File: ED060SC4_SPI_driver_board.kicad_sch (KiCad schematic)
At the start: 38 parts, among them J2 Conn_01x06, J3 Conn_01x04, J4 Conn_01x04, J5 Conn_01x06, SW1 SS12D07VG2, SW2 DSIC01LSGET, U2 STM32F103C8T6, U3 USBLC6-4SC6, U4 USBLC6-2SC6, U5 USBLC6-2SC6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

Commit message: TPS Connector and LCSC part #
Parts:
- added J6: Conn_01x02, Connector_PinSocket_2.54mm:PinSocket_1x02_P2.54mm_Vertical, symbol Connector_Generic:Conn_01x02
- C20, C21, C22, C23, C28: LCSC Part # (none) -> C1591
- C24: LCSC Part # (none) -> C85713
- C25: LCSC Part # (none) -> C1589
- C26, C27: LCSC Part # (none) -> C5673
- C29, C30: LCSC Part # (none) -> C1634
- D2: LCSC Part # (none) -> C82544
- FB1: LCSC Part # (none) -> C14709
- R10, R12, R14: LCSC Part # (none) -> C98220
- R3: LCSC Part # (none) -> C22548
- R5: LCSC Part # (none) -> C103196
- SW1: LCSC Part # (none) -> C2939724
- SW2: LCSC Part # (none) -> C54948
- U2: LCSC Part # (none) -> C8734
- U3: LCSC Part # (none) -> C5197386
- U4, U5: LCSC Part # (none) -> C2827654
- Y1: LCSC Part # (none) -> C112972
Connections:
- net SWCLK: no longer J4.2 (Pin_2), U4.3 (I/O2)
- net SWDIO: no longer J4.3 (Pin_3), U4.1 (I/O1)
- net TPS_PWRUP: now also J6.1 (Pin_1)
- net TPS_WAKEUP: now also J6.2 (Pin_2)
- net USART1_RX: no longer J3.3 (Pin_3), U5.1 (I/O1)
- net USART1_TX: no longer J3.2 (Pin_2), U5.3 (I/O2)
- new net SWCLK_conn: J4.2 (Pin_2), U4.3 (I/O2)
- new net SWDIO_conn: J4.3 (Pin_3), U4.1 (I/O1)
- new net USART1_RX_conn: J3.3 (Pin_3), U5.1 (I/O1)
- new net USART1_TX_conn: J3.2 (Pin_2), U5.3 (I/O2)
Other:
- moved on the sheet: TP8, TP9

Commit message: Updated TPS pad for heat dissipation
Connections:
- net PWR_ON_LED_1: now reaches R3.1, SW2.2
- net PWR_ON_LED renamed PWR_ON_LED_0
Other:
- moved on the sheet: R3
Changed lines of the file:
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@@
+    (stroke (width 0) (type default))
+  )
+  (wire (pts (xy 81.28 55.88) (xy 81.28 52.07))
     (stroke (width 0) (type default))
   )
@@
     (stroke (width 0) (type default))
   )
+  (wire (pts (xy 190.5 88.9) (xy 208.28 88.9))
+    (stroke (width 0) (type default))
+  )
+  (wire (pts (xy 16.51 109.22) (xy 31.75 109.22))
+    (stroke (width 0) (type default))
+  )
+  (wire (pts (xy 24.13 55.88) (xy 36.83 55.88))
+    (stroke (width 0) (type default))
+  )
+  (wire (pts (xy 190.5 86.36) (xy 208.28 86.36))
+    (stroke (width 0) (type default))
+  )
   (wire (pts (xy 72.39 36.83) (xy 81.28 36.83))
-    (stroke (width 0) (type default))
-  )
-  (wire (pts (xy 190.5 88.9) (xy 208.28 88.9))
-    (stroke (width 0) (type default))
-  )
-  (wire (pts (xy 16.51 109.22) (xy 31.75 109.22))
-    (stroke (width 0) (type default))
-  )
-  (wire (pts (xy 24.13 55.88) (xy 36.83 55.88))
-    (stroke (width 0) (type default))
-  )
-  (wire (pts (xy 190.5 86.36) (xy 208.28 86.36))
     (stroke (width 0) (type default))
   )
@@
     (effects (font (size 1.27 1.27)) (justify right bottom))
   )
-  (label "PWR_ON_LED" (at 74.93 36.83 0) (fields_autoplaced)
+  (label "PWR_ON_LED_0" (at 73.66 36.83 0) (fields_autoplaced)
     (effects (font (size 0.7 0.7)) (justify left bottom))
   )
@@
   (label "SPI1_MISO" (at 36.83 53.34 180) (fields_autoplaced)
     (effects (font (size 1.27 1.27)) (justify right bottom))
+  )
+  (label "PWR_ON_LED_1" (at 81.28 53.34 180) (fields_autoplaced)
+    (effects (font (size 0.7 0.7)) (justify right bottom))
   )
   (label "D3" (at 270.51 129.54 180) (fields_autoplaced)
@@
     )
   )
-  (symbol (lib_id "power:GND") (at 81.28 59.69 0) (unit 1)
+  (symbol (lib_id "power:GND") (at 81.28 63.5 0) (unit 1)
     (in_bom yes) (on_board yes) (dnp no) (fields_autoplaced)
-    (property "Reference" "#PWR077" (at 81.28 66.04 0)
-      (effects (font (size 1.27 1.27)) hide)
-    )
-    (property "Value" "GND" (at 81.28 64.77 0)
-      (effects (font (size 1.27 1.27)) hide)
-    )
-    (property "Footprint" "" (at 81.28 59.69 0)
-      (effects (font (size 1.27 1.27)) hide)
-    )
-    (property "Datasheet" "" (at 81.28 59.69 0)
+    (property "Reference" "#PWR077" (at 81.28 69.85 0)
+      (effects (font (size 1.27 1.27)) hide)
+    )
+    (property "Value" "GND" (at 81.28 68.58 0)
+      (effects (font (size 1.27 1.27)) hide)
+    )
+    (property "Footprint" "" (at 81.28 63.5 0)
+      (effects (font (size 1.27 1.27)) hide)
+    )
+    (property "Datasheet" "" (at 81.28 63.5 0)
       (effects (font (size 1.27 1.27)) hide)
     )
@@
     )
   )
-  (symbol (lib_id "Device:R") (at 81.28 55.88 0) (unit 1)
-    (in_bom yes) (on_board yes) (dnp no)
-    (property "Reference" "R3" (at 82.55 54.61 0)
-      (effects (font (size 1.27 1.27)) (justify left))
-    )
-    (property "Value" "1k" (at 82.55 57.15 0)
-      (effects (font (size 1.27 1.27)) (justify left))
-    )
-    (property "Footprint" "Resistor_SMD:R_0603_1608Metric" (at 79.502 55.88 90)
-      (effects (font (size 1.27 1.27)) hide)
-    )
-    (property "Datasheet" "~" (at 81.28 55.88 0)
-      (effects (font (size 1.27 1.27)) hide)
-    )
-    (property "LCSC Part #" "C22548" (at 81.28 55.88 0)
-      (effects (font (size 1.27 1.27)) hide)
-    )
+  (symbol (lib_id "Device:R") (at 81.28 59.69 0) (unit 1)
+    (in_bom yes) (on_board yes) (dnp no)
+    (property "Reference" "R3" (at 82.55 58.42 0)
+      (effects (font (size 1.27 1.27)) (justify left))
+    )
+    (property "Value" "1k" (at 82.55 60.96 0)
+      (effects (font (size 1.27 1.27)) (justify left))
+    )
+    (property "Footprint" "Resistor_SMD:R_0603_1608Metric" (at 79.502 59.69 90)
+      (effects (font (size 1.27 1.27)) hide)
+    )
+    (property "Datasheet" "~" (at 81.28 59.69 0)
+      (effects (font (size 1.27 1.27)) hide)
+    )
+    (property "LCSC Part #" "C22548" (at 81.28 59.69 0)
+      (effects (font (size 1.27 1.27)) hide)
+    )

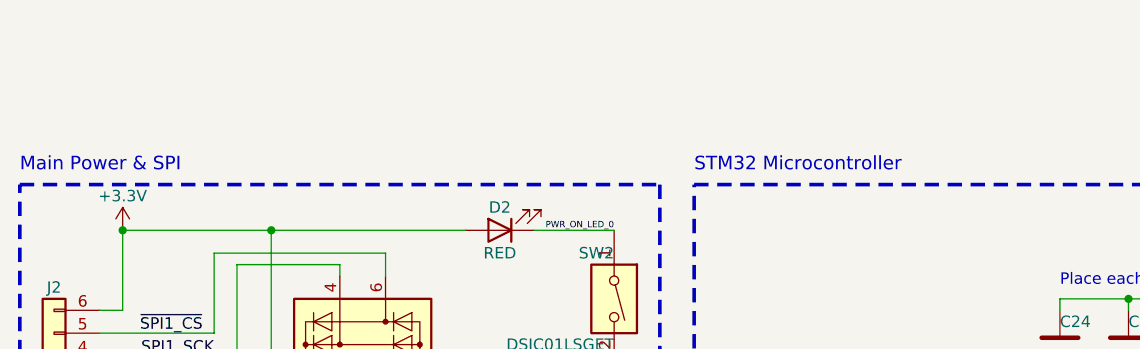
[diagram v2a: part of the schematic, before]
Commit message: Add titles to schematics
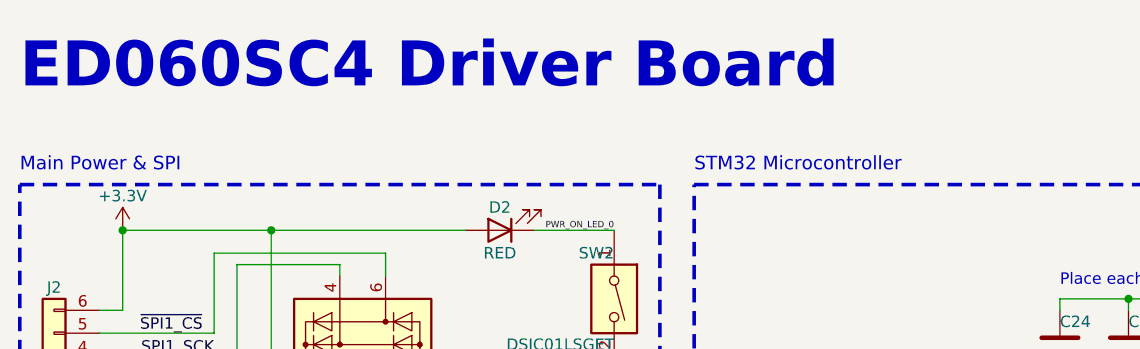
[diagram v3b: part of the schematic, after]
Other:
- note added: "ED060SC4 Driver Board"
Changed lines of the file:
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@@
     (effects (font (size 1.27 1.27)) (justify left bottom))
+  )
+  (text "ED060SC4 Driver Board\n" (at 15.24 21.59 0)
+    (effects (font (size 5 5) (thickness 1.2) bold) (justify left bottom))
   )
   (text "Serial Wire Debug\n\n" (at 15.24 165.1 0)

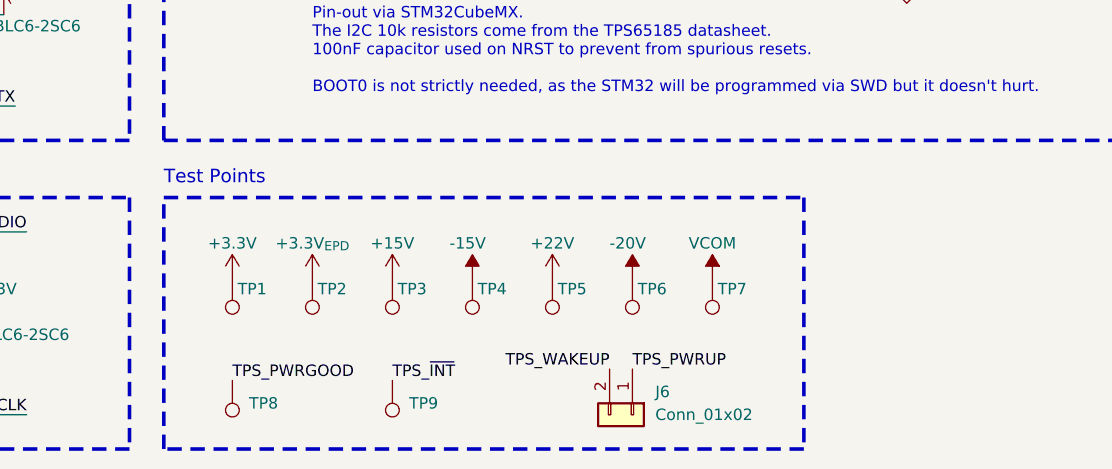
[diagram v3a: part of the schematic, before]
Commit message: Add mounting holes
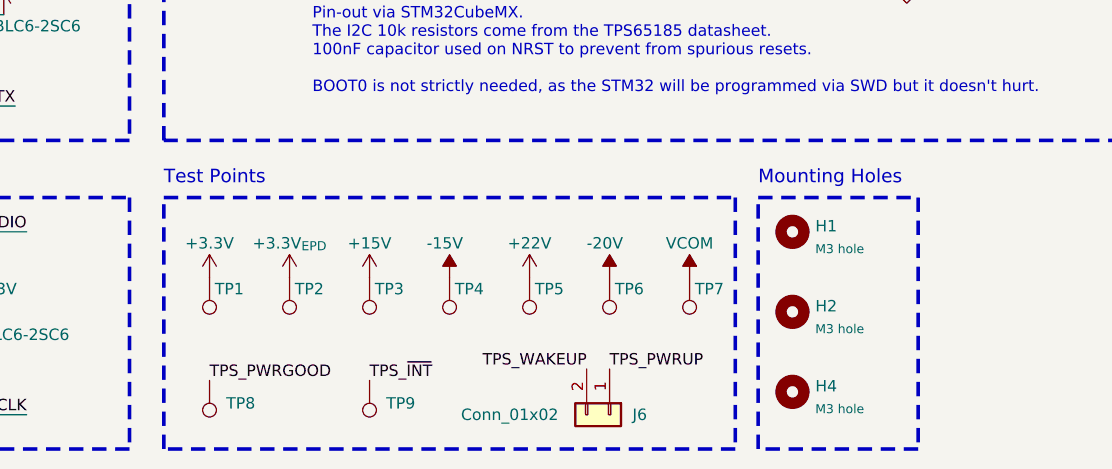
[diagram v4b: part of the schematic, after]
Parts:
- added H1, H2, H4: M3 hole, MountingHole:MountingHole_2.2mm_M2, symbol Mechanical:MountingHole
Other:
- note added: "Mounting Holes"
- moved on the sheet: J6, TP1, TP2, TP3, TP4, TP5, TP6, TP7, TP8, TP9

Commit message: Fix LED BOM # and update outputs
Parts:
- D2: LCSC Part # C82544 -> C434419
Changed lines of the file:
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@@
       (effects (font (size 1.27 1.27)) hide)
     )
-    (property "LCSC Part #" "C82544" (at 68.58 36.83 0)
+    (property "LCSC Part #" "C434419" (at 68.58 36.83 0)
       (effects (font (size 1.27 1.27)) hide)
     )

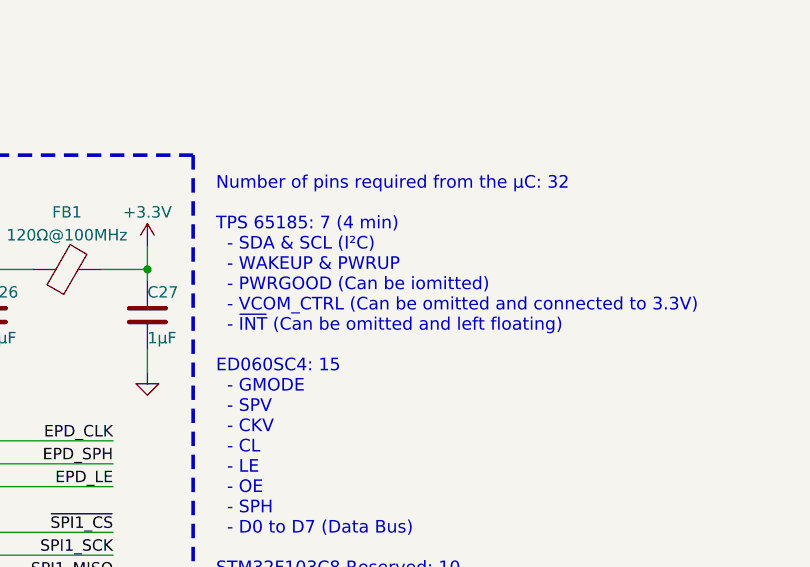
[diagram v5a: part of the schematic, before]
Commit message: Add VN pad under TPS and fix some typos
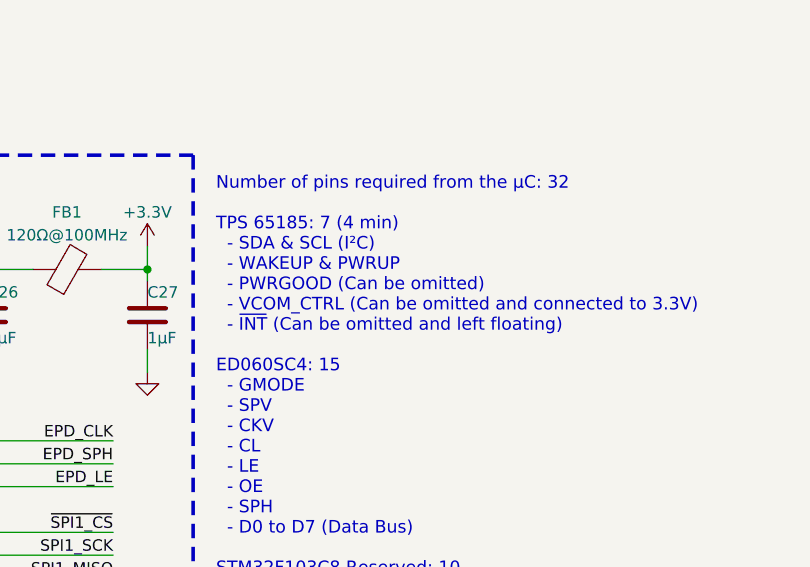
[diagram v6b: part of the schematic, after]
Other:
- note added: "Number of pins required from the µC: 32 TPS 65185: 7 (4 min) - SDA & SCL (I²C) - WAKEUP & PWRUP - PWRGOOD (Can be omitted) - VCOM_CTRL (Can be omitted and connected to 3.3V) - ~{INT} (Can be omitted and left floating) ED060SC4: 15 - GMODE - SPV - CKV - CL - LE - OE - SPH - D0 to D7 (Data Bus) STM32F103C8 Reserved: 10 - SWD (SWCLK, SWDIO) - USART (RX, TX) - SPI (SCK, MOSI, MISO, CS) - Oscillator (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"
- note removed: "Number of pins required from the µC: 32 TPS 65185: 7 (4 min) - SDA & SCL (I²C) - WAKEUP & PWRUP - PWRGOOD (Can be iomitted) - VCOM_CTRL (Can be omitted and connected to 3.3V) - ~{INT} (Can be omitted and left floating) ED060SC4: 15 - GMODE - SPV - CKV - CL - LE - OE - SPH - D0 to D7 (Data Bus) STM32F103C8 Reserved: 10 - SWD (SWCLK, SWDIO) - USART (RX, TX) - SPI (SCK, MOSI, MISO, CS) - Oscillator 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"
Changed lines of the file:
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@@
     (fill (type none))
   )
-  (text "Number of pins required from the µC: 32\n\nTPS 65185: 7 (4 min)\n  - SDA & SCL (I²C)\n  - WAKEUP & PWRUP\n  - PWRGOOD (Can be iomitted)\n  - VCOM_CTRL (Can be omitted and connected to 3.3V)\n  - ~{INT} (Can be omitted and left floating)\n\nED060SC4: 15\n  - GMODE\n  - SPV\n  - CKV\n  - CL\n  - LE\n  - OE\n  - SPH\n  - D0 to D7 (Data Bus)\n\nSTM32F103C8 Reserved: 10\n  - SWD (SWCLK, SWDIO)\n  - USART (RX, TX)\n  - SPI (SCK, MOSI, MISO, CS)\n  - Oscillator (OSC_IN, OSC_OUT)"
+  (text "Number of pins required from the µC: 32\n\nTPS 65185: 7 (4 min)\n  - SDA & SCL (I²C)\n  - WAKEUP & PWRUP\n  - PWRGOOD (Can be omitted)\n  - VCOM_CTRL (Can be omitted and connected to 3.3V)\n  - ~{INT} (Can be omitted and left floating)\n\nED060SC4: 15\n  - GMODE\n  - SPV\n  - CKV\n  - CL\n  - LE\n  - OE\n  - SPH\n  - D0 to D7 (Data Bus)\n\nSTM32F103C8 Reserved: 10\n  - SWD (SWCLK, SWDIO)\n  - USART (RX, TX)\n  - SPI (SCK, MOSI, MISO, CS)\n  - Oscillator (OSC_IN, OSC_OUT)"
     (at 219.71 87.63 0)
     (effects (font (size 1.4 1.4)) (justify left bottom))
